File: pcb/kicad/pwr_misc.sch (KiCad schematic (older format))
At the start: 4 parts, among them U10 MCP1824-2.5, U7 LT1117-3.3, U8 LT1117-1.2, U9 MCP1824-1.8

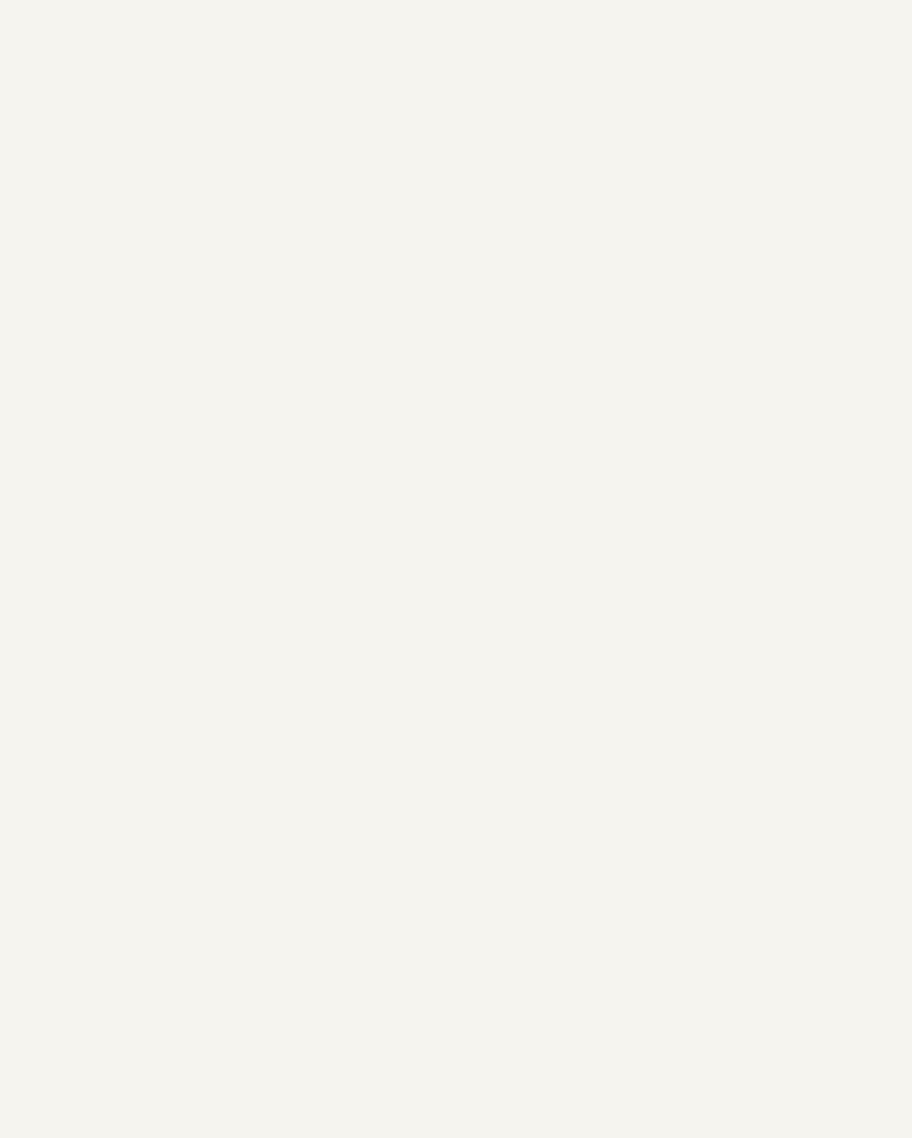
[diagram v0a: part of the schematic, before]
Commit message: clean up AVR code(deprecated), kicad libs, pcb WIP
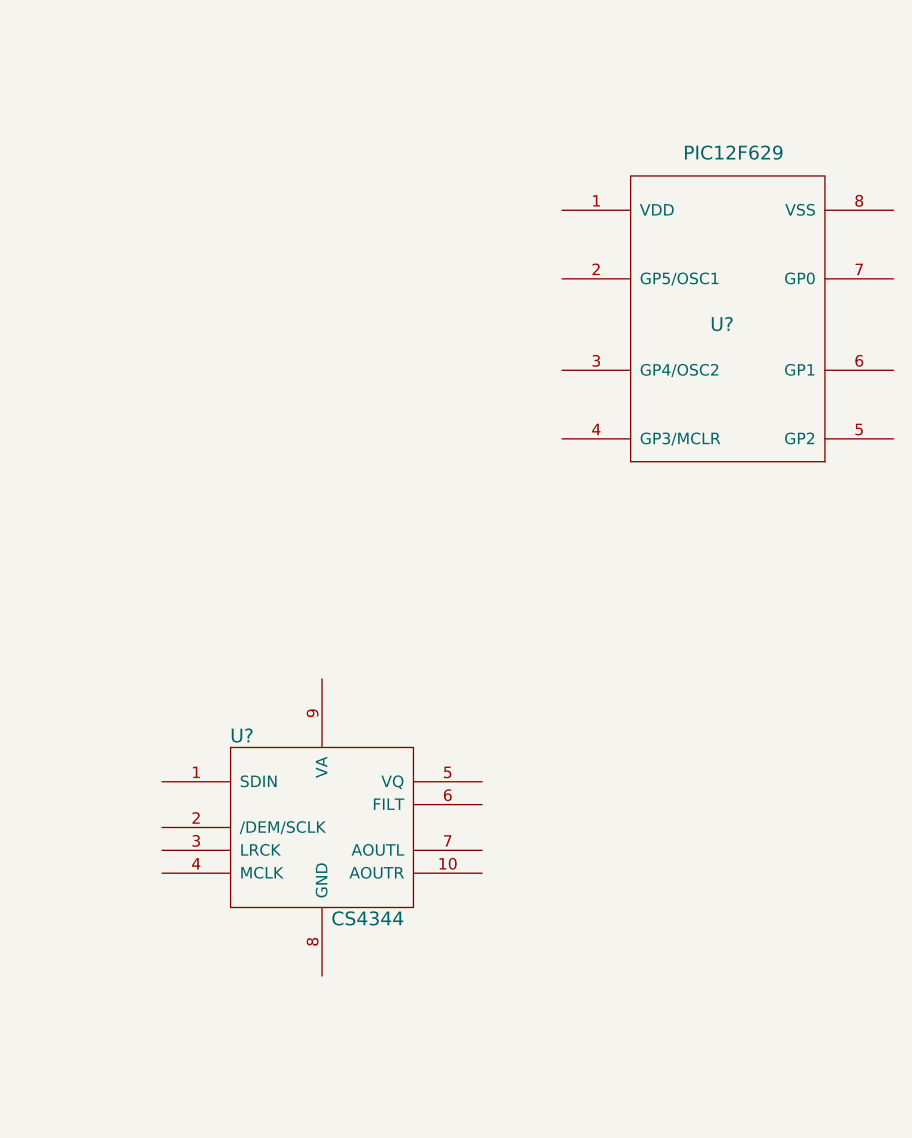
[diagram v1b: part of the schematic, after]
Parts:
- added U?: PIC12F629, symbol PIC12F629
- added U?: CS4344, symbol CS4344
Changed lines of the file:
@@
-EESchema Schematic File Version 2  date Tue 09 Feb 2010 11:25:34 PM CET
+EESchema Schematic File Version 2  date Wed 24 Mar 2010 11:33:24 PM CET
 LIBS:sd2snes-cache
 LIBS:power
@@
 LIBS:lpc1754
 LIBS:sdcard
-LIBS:testsw
+LIBS:sd_card
+LIBS:cy62148ev30
+LIBS:mt45w8mw16
+LIBS:cs4344
 EELAYER 24  0
 EELAYER END
 $Descr A4 11700 8267
-Sheet 3 5
+Sheet 3 6
 Title ""
 Date "9 feb 2010"
@@
 $EndDescr
 $Comp
+L CS4344 U?
+U 1 1 4BAA9331
+P 6650 4850
+F 0 "U?" H 6300 5250 60  0000 C CNN
+F 1 "CS4344" H 6850 4450 60  0000 C CNN
+	1    6650 4850
+	1    0    0    -1
+$EndComp
+$Comp
+L PIC12F629 U?
+U 1 1 4BAA92DB
+P 8450 2650
+F 0 "U?" H 8400 2650 60  0000 C CNN
+F 1 "PIC12F629" H 8450 3400 60  0000 C CNN
+	1    8450 2650
+	1    0    0    -1
+$EndComp
+$Comp
 L GND #PWR01

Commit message: kicad wip
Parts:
- added C1, C2: 10u, symbol C
- added C3, C4, C7, C8: 4.7u, symbol C
- added C32, C33: 100n, symbol C
- added C5, C6: 100u, symbol CP1
- gave numbers to parts that had none: 2
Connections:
- net +1.2V: now also C6.1
- net +1.8V: now also C7.1
- net +2.5V: now also C8.1
- net +3.3V: now also U14.9 (VA), C2.1, C3.1, C33.1, C4.1, C5.1
- net +5V: now also U15.1 (VDD), C1.1, C32.1
- net GND: now also U14.8 (GND), U15.8 (VSS), C1.2, C2.2, C3.2, C32.2, C33.2, C4.2, C5.2, C6.2, C7.2, C8.2
- net CIC_CLK: now reaches U15.2 (GP5/OSC1)
- net CIC_STATUS: now reaches U15.3 (GP4/OSC2)
- net CIC_MCLR: now reaches U15.4 (GP3/MCLR)
- net CIC_RESET: now reaches U15.5 (GP2)
- net CIC_DATA1: now reaches U15.6 (GP1)
- net CIC_DATA0: now reaches U15.7 (GP0)
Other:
- note added: "Audio DAC"
- note added: "CIC Clone"
- note added: "Power Supply"
- moved on the sheet: U14, U15

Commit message: Schematics+PCB WIP
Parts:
- added BT1: BATTERY, symbol BATTERY
- added D1: DOUBLE_SCH_KCOM2, symbol DOUBLE_SCH_KCOM2
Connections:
- net +1.2V: now also U8.4 (Vout)
- net +3.3V: now also U7.4 (Vout)
- net GND: now also BT1.2 (-)
- net DAC_SDIN: now reaches U14.1 (SDIN)
- net DAC_LRCK: now reaches U14.3 (LRCK)
- net DAC_MCLK: now reaches U14.4 (MCLK)
- new net +BATT: BT1.1 (+)
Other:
- moved on the sheet: U14, U15

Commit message: pcb wip
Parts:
- D1: value DOUBLE_SCH_KCOM2 -> BAT54C
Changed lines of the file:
@@
-EESchema Schematic File Version 2  date Sat 15 May 2010 02:07:58 AM CEST
+EESchema Schematic File Version 2  date Sat 15 May 2010 04:06:22 PM CEST
 LIBS:power
 LIBS:device
@@
 Sheet 5 6
 Title "sd2snes Mark II"
-Date "14 may 2010"
+Date "15 may 2010"
 Rev "A"
 Comp "Maximilian Rehkopf"
@@
 P 5950 5300
 F 0 "D1" H 6100 5175 60  0000 C CNN
-F 1 "DOUBLE_SCH_KCOM2" H 5950 5450 60  0000 C CNN
+F 1 "BAT54C" H 5950 5450 60  0000 C CNN
 	1    5950 5300
 	1    0    0    -1
